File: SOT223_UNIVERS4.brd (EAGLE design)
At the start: 5 parts

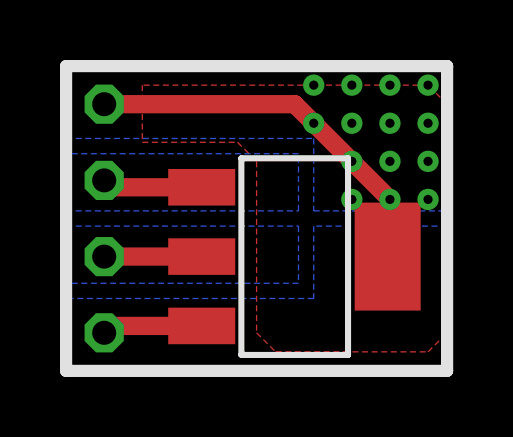
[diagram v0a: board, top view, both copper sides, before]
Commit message: adjusted trace widths
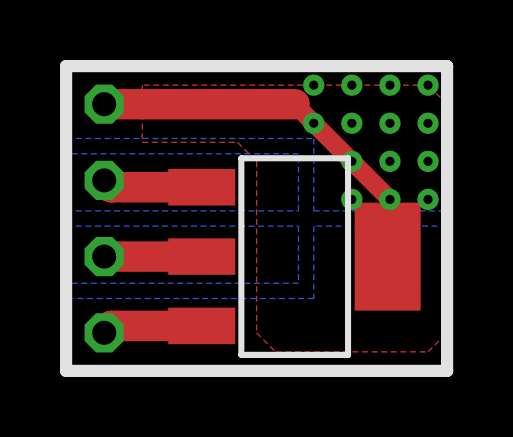
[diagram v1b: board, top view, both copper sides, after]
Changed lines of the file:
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@@
 <grid distance="0.05" unitdist="inch" unit="mm" style="lines" multiple="1" display="yes" altdistance="0.025" altunitdist="inch" altunit="mm"/>
 <layers>
-<layer number="1" name="Top" color="4" fill="1" visible="yes" active="yes"/>
+<layer number="1" name="Top" color="4" fill="1" visible="no" active="yes"/>
 <layer number="2" name="Route2" color="1" fill="3" visible="no" active="no"/>
 <layer number="3" name="Route3" color="4" fill="3" visible="no" active="no"/>
@@
 <layer number="19" name="Unrouted" color="6" fill="1" visible="yes" active="yes"/>
 <layer number="20" name="Dimension" color="15" fill="1" visible="yes" active="yes"/>
-<layer number="21" name="tPlace" color="7" fill="1" visible="yes" active="yes"/>
+<layer number="21" name="tPlace" color="7" fill="1" visible="no" active="yes"/>
 <layer number="22" name="bPlace" color="7" fill="1" visible="yes" active="yes"/>
-<layer number="23" name="tOrigins" color="15" fill="1" visible="yes" active="yes"/>
+<layer number="23" name="tOrigins" color="15" fill="1" visible="no" active="yes"/>
 <layer number="24" name="bOrigins" color="15" fill="1" visible="yes" active="yes"/>
-<layer number="25" name="tNames" color="7" fill="1" visible="yes" active="yes"/>
+<layer number="25" name="tNames" color="7" fill="1" visible="no" active="yes"/>
 <layer number="26" name="bNames" color="7" fill="1" visible="yes" active="yes"/>
-<layer number="27" name="tValues" color="7" fill="1" visible="yes" active="yes"/>
-<layer number="28" name="bValues" color="7" fill="1" visible="yes" active="yes"/>
+<layer number="27" name="tValues" color="7" fill="1" visible="no" active="yes"/>
+<layer number="28" name="bValues" color="7" fill="1" visible="no" active="yes"/>
 <layer number="29" name="tStop" color="7" fill="3" visible="no" active="yes"/>
-<layer number="30" name="bStop" color="7" fill="6" visible="no" active="yes"/>
+<layer number="30" name="bStop" color="7" fill="6" visible="yes" active="yes"/>
 <layer number="31" name="tCream" color="7" fill="4" visible="no" active="yes"/>
 <layer number="32" name="bCream" color="7" fill="5" visible="no" active="yes"/>
@@
 <layer number="37" name="tTest" color="7" fill="1" visible="no" active="yes"/>
 <layer number="38" name="bTest" color="7" fill="1" visible="no" active="yes"/>
-<layer number="39" name="tKeepout" color="4" fill="11" visible="yes" active="yes"/>
+<layer number="39" name="tKeepout" color="4" fill="11" visible="no" active="yes"/>
 <layer number="40" name="bKeepout" color="1" fill="11" visible="yes" active="yes"/>
-<layer number="41" name="tRestrict" color="4" fill="10" visible="yes" active="yes"/>
+<layer number="41" name="tRestrict" color="4" fill="10" visible="no" active="yes"/>
 <layer number="42" name="bRestrict" color="1" fill="10" visible="yes" active="yes"/>
 <layer number="43" name="vRestrict" color="2" fill="10" visible="yes" active="yes"/>
 <layer number="44" name="Drills" color="7" fill="1" visible="no" active="yes"/>
 <layer number="45" name="Holes" color="7" fill="1" visible="no" active="yes"/>
-<layer number="46" name="Milling" color="3" fill="1" visible="no" active="yes"/>
+<layer number="46" name="Milling" color="3" fill="1" visible="yes" active="yes"/>
 <layer number="47" name="Measures" color="7" fill="1" visible="no" active="yes"/>
-<layer number="48" name="Document" color="7" fill="1" visible="yes" active="yes"/>
-<layer number="49" name="Reference" color="7" fill="1" visible="yes" active="yes"/>
-<layer number="51" name="tDocu" color="7" fill="1" visible="yes" active="yes"/>
-<layer number="52" name="bDocu" color="7" fill="1" visible="yes" active="yes"/>
+<layer number="48" name="Document" color="7" fill="1" visible="no" active="yes"/>
+<layer number="49" name="Reference" color="7" fill="1" visible="no" active="yes"/>
+<layer number="51" name="tDocu" color="7" fill="1" visible="no" active="yes"/>
+<layer number="52" name="bDocu" color="7" fill="1" visible="no" active="yes"/>
 <layer number="91" name="Nets" color="2" fill="1" visible="no" active="no"/>
 <layer number="92" name="Busses" color="1" fill="1" visible="no" active="no"/>
@@
 <layer number="97" name="Info" color="7" fill="1" visible="no" active="no"/>
 <layer number="98" name="Guide" color="6" fill="1" visible="no" active="no"/>
-<layer number="125" name="_tNames" color="14" fill="1" visible="yes" active="yes"/>
-<layer number="126" name="_bNames" color="5" fill="1" visible="yes" active="yes"/>
+<layer number="125" name="_tNames" color="14" fill="1" visible="no" active="yes"/>
+<layer number="126" name="_bNames" color="5" fill="1" visible="no" active="yes"/>
 <layer number="200" name="200bmp" color="1" fill="10" visible="no" active="no"/>
 </layers>
@@
 <contactref element="E$80" pad="4"/>
 <contactref element="E$58" pad="P$1"/>
-<wire x1="1.27" y1="8.89" x2="7.62" y2="8.89" width="0.6096" layer="1"/>
+<wire x1="1.27" y1="8.89" x2="7.62" y2="8.89" width="1.016" layer="1"/>
 <wire x1="7.62" y1="8.89" x2="10.795" y2="5.715" width="0.6096" layer="1"/>
 <wire x1="10.795" y1="5.715" x2="10.795" y2="3.886" width="0.6096" layer="1"/>
@@
 <contactref element="E$287" pad="P$1"/>
 <contactref element="E$80" pad="2"/>
-<wire x1="1.27" y1="3.81" x2="4.521" y2="3.81" width="0.6096" layer="1"/>
+<wire x1="1.27" y1="3.81" x2="4.521" y2="3.81" width="1.016" layer="1"/>
 <polygon width="0.254" layer="16">
 <vertex x="0" y="2.921"/>
@@
 <contactref element="E$80" pad="1"/>
 <contactref element="E$286" pad="P$1"/>
-<wire x1="1.27" y1="6.35" x2="1.499" y2="6.121" width="0.6096" layer="1"/>
-<wire x1="1.499" y1="6.121" x2="4.521" y2="6.121" width="0.6096" layer="1"/>
+<wire x1="1.27" y1="6.35" x2="1.499" y2="6.121" width="1.016" layer="1"/>
+<wire x1="1.499" y1="6.121" x2="4.521" y2="6.121" width="1.016" layer="1"/>
 <polygon width="0.254" layer="16">
 <vertex x="0" y="7.239"/>
@@
 <contactref element="E$80" pad="3"/>
 <contactref element="E$288" pad="P$1"/>
-<wire x1="1.27" y1="1.27" x2="1.499" y2="1.499" width="0.6096" layer="1"/>
-<wire x1="1.499" y1="1.499" x2="4.521" y2="1.499" width="0.6096" layer="1"/>
+<wire x1="1.27" y1="1.27" x2="1.499" y2="1.499" width="1.016" layer="1"/>
+<wire x1="1.499" y1="1.499" x2="4.521" y2="1.499" width="1.016" layer="1"/>
 <polygon width="0.254" layer="16">
 <vertex x="0" y="2.413"/>
